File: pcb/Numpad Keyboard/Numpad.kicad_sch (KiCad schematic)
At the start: 57 parts, among them U1 MCP23S17_SO, U2 IS31FL3743-QF

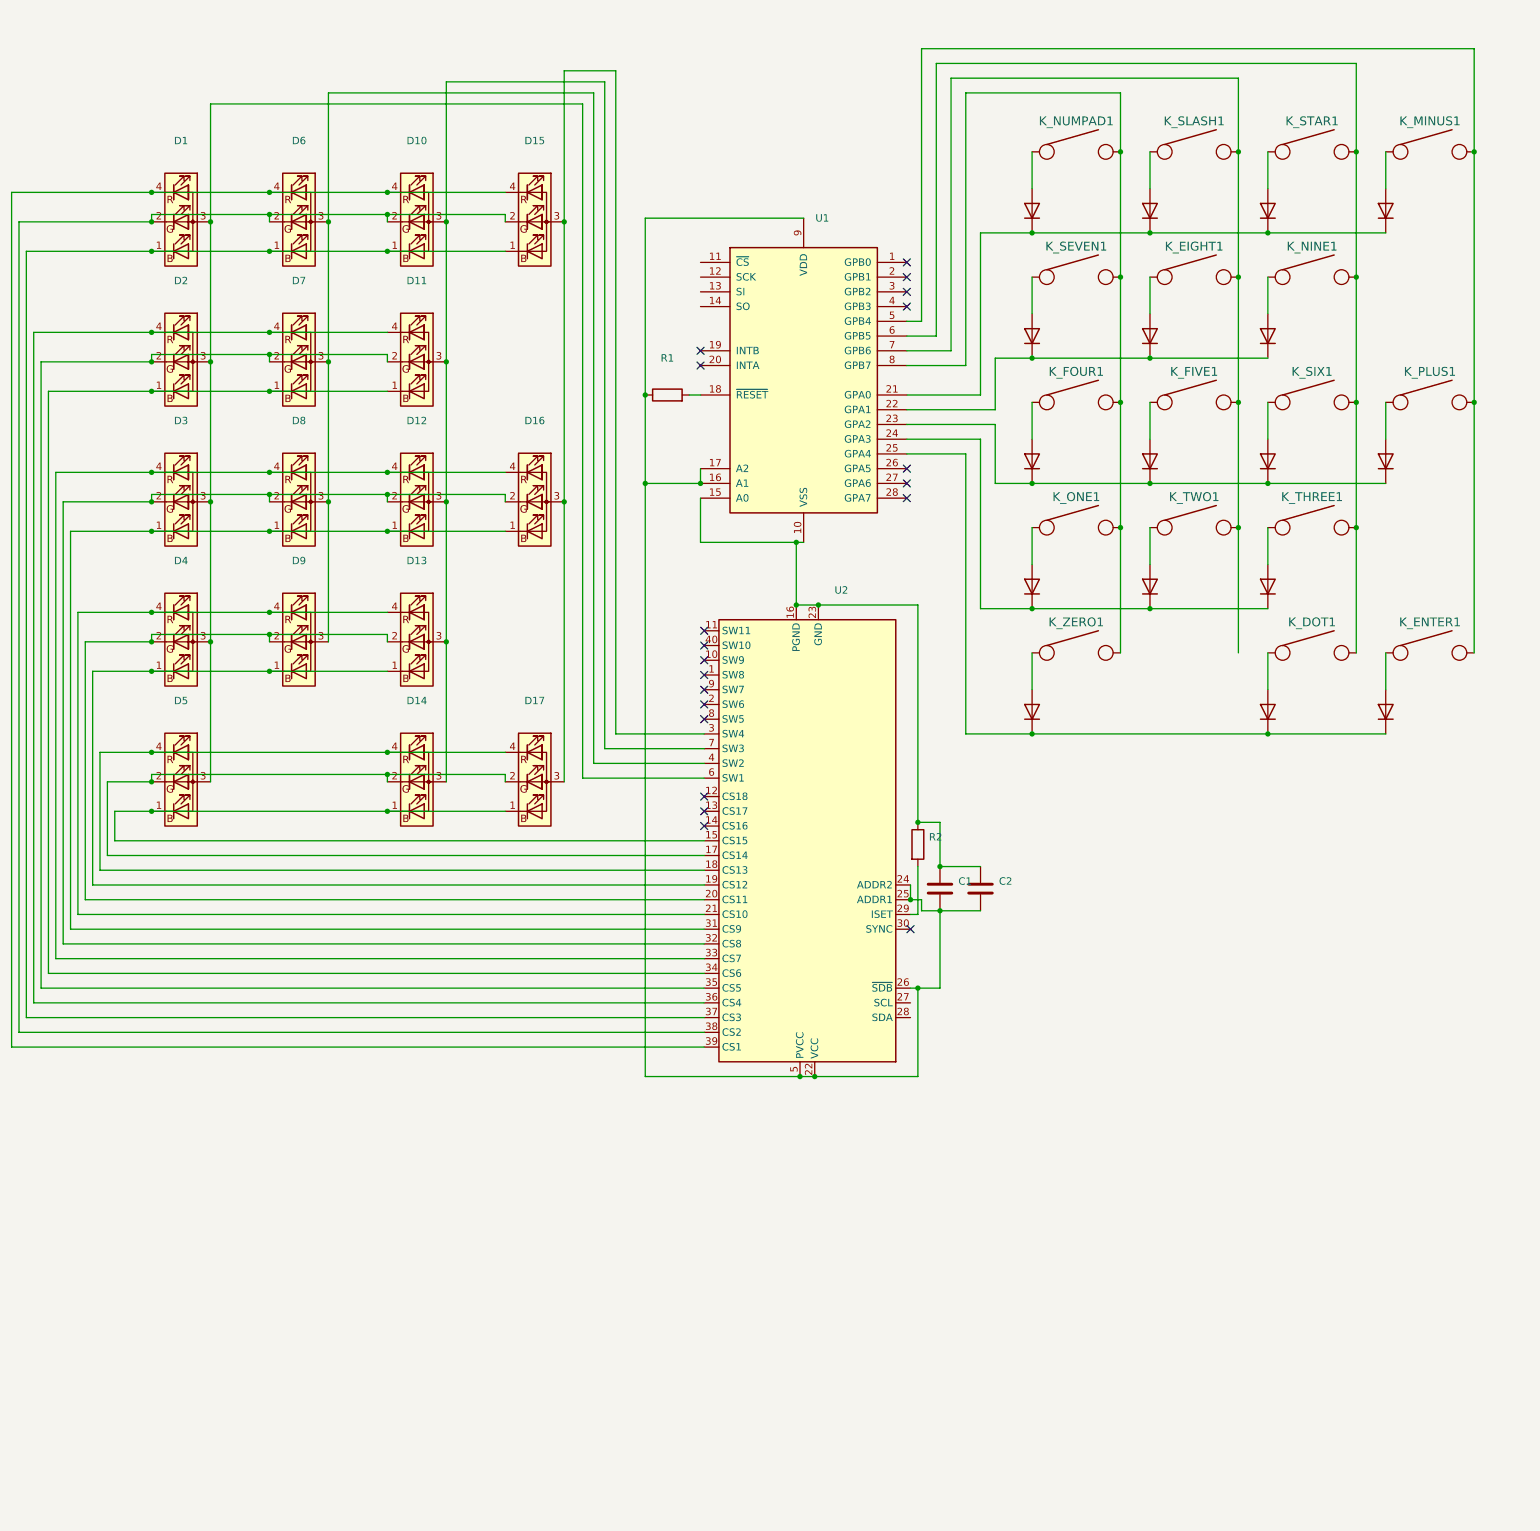
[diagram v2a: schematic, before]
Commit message: Added second LED controller for higher current per LED
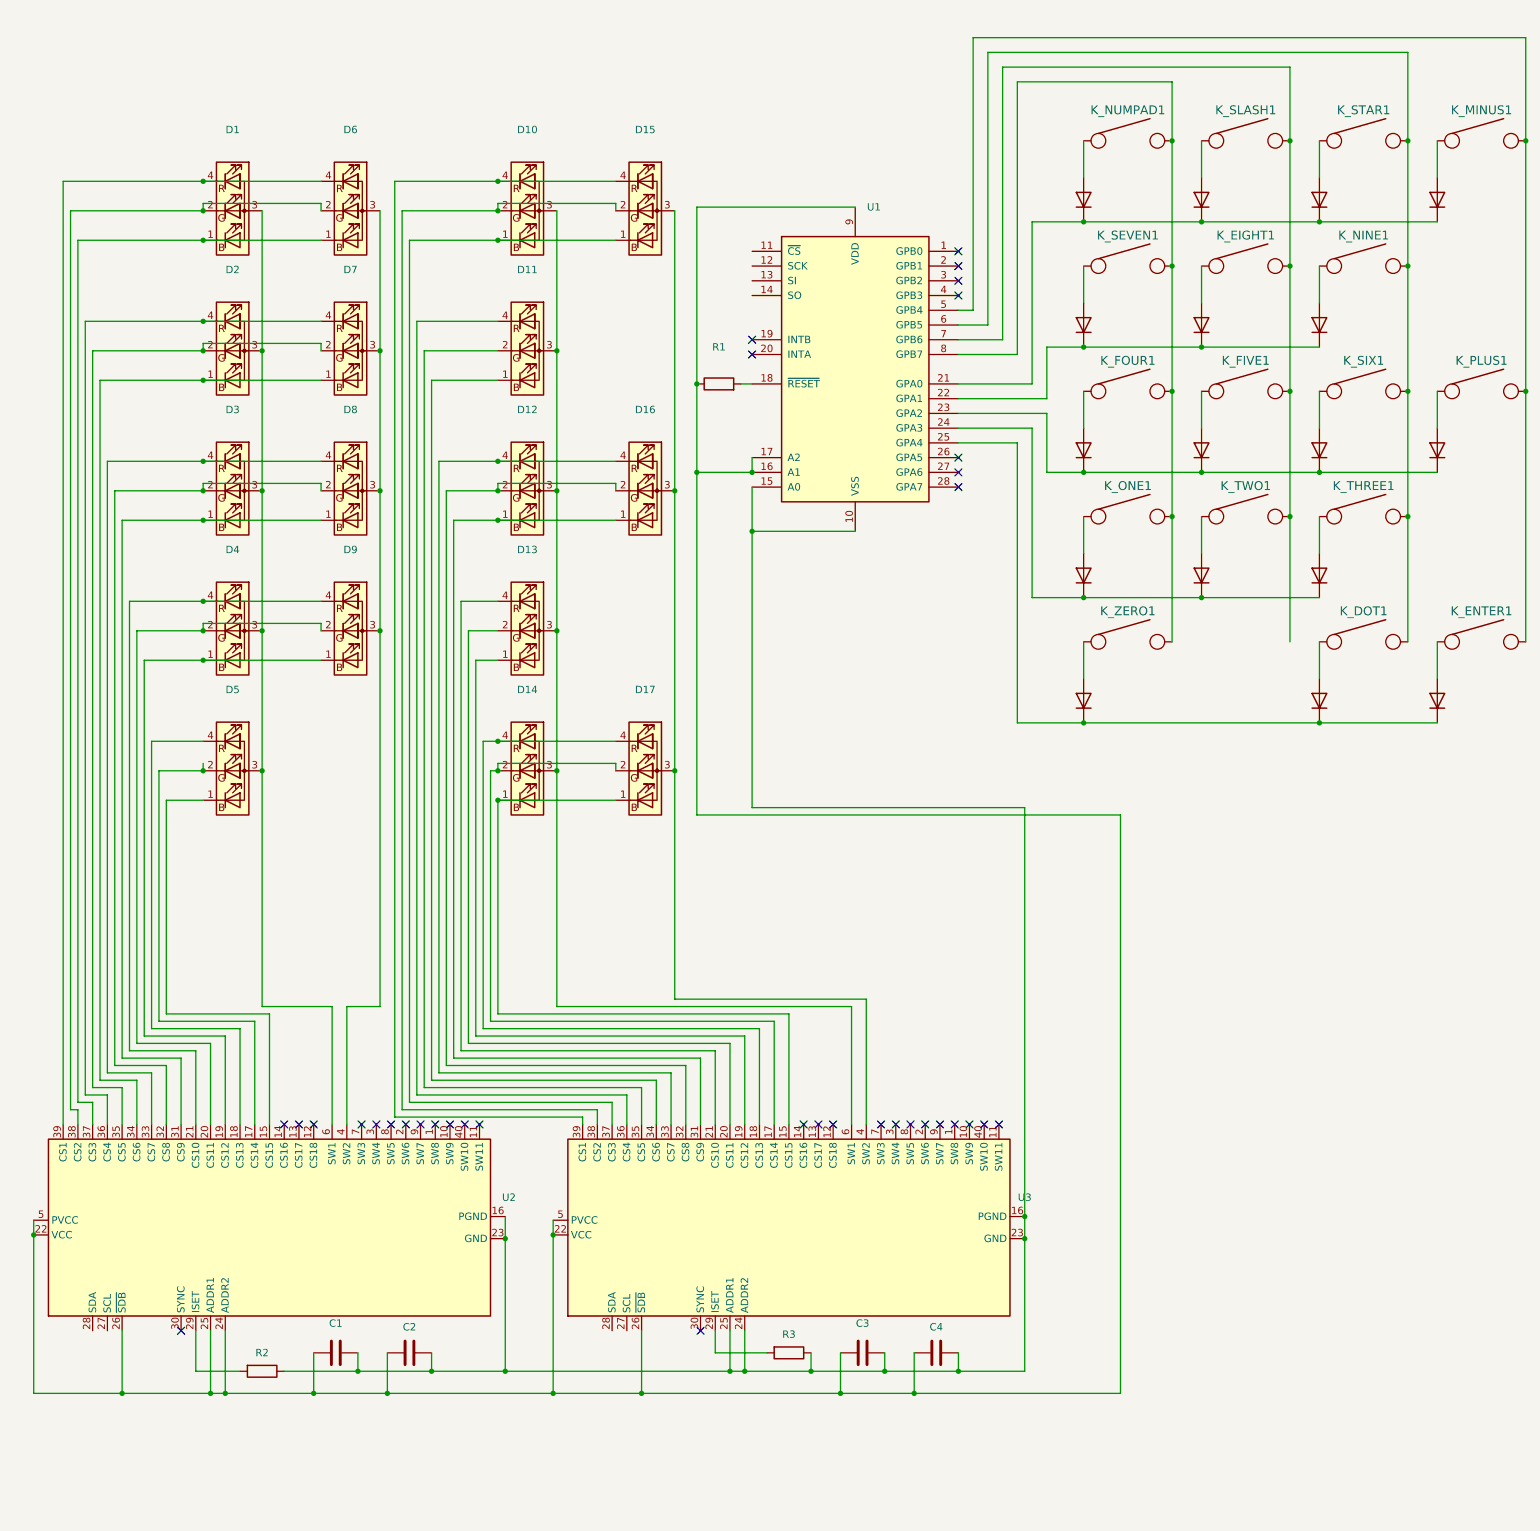
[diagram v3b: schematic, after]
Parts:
- added C3: C 1uF, Footprints:C_0402_1005Metric, symbol vakeyboard:C 1uF
- added C4: C_100nF, Footprints:C_0402_1005Metric, symbol vakeyboard:C_100nF
- added R3: R, Footprints:R_0402_1005Metric, symbol vakeyboard:R
- added U3: IS31FL3743-QF, Footprints:QFN-40-1EP_5x5mm_P0.4mm_EP3.4x3.4mm, symbol vakeyboard:IS31FL3743-QF
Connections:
- net at D1.1 (BK), D6.1 (BK), U2.37 (CS3): no longer D10.1 (BK), D15.1 (BK)
- net at D1.2 (GK), D6.2 (GK), U2.38 (CS2): no longer D10.2 (GK), D15.2 (GK)
- net at D1.4 (RK), D6.4 (RK), U2.39 (CS1): no longer D10.4 (RK), D15.4 (RK)
- net at D2.1 (BK), D7.1 (BK), U2.34 (CS6): no longer D11.1 (BK)
- net at D2.2 (GK), D7.2 (GK), U2.35 (CS5): no longer D11.2 (GK)
- net at D2.4 (RK), D7.4 (RK), U2.36 (CS4): no longer D11.4 (RK)
- net at D15.3 (A), D16.3 (A), D17.3 (A): now also U3.4 (SW2); no longer U2.3 (SW4)
- net at D3.1 (BK), D8.1 (BK), U2.31 (CS9): no longer D12.1 (BK), D16.1 (BK)
- net at D3.2 (GK), D8.2 (GK), U2.32 (CS8): no longer D12.2 (GK), D16.2 (GK)
- net at D3.4 (RK), D8.4 (RK), U2.33 (CS7): no longer D12.4 (RK), D16.4 (RK)
- net at D4.1 (BK), D9.1 (BK), U2.19 (CS12): no longer D13.1 (BK)
- net at D4.2 (GK), D9.2 (GK), U2.20 (CS11): no longer D13.2 (GK)
- net at D4.4 (RK), D9.4 (RK), U2.21 (CS10): no longer D13.4 (RK)
- net at R2.1, U1.10 (VSS), U1.15 (A0)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: now also C1.2, C2.2, C3.2, C4.2, R3.1, U3.16 (PGND), U3.23 (GND), U3.24 (ADDR2), U3.25 (ADDR1); no longer C1.1, C2.1
- net at R1.1, U1.16 (A1), U1.17 (A2)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: now also C1.1, C2.1, C3.1, C4.1, U3.22 (VCC), U3.26 (~{SDB}), U3.5 (PVCC); no longer C1.2, C2.2
- net at D10.3 (A), D11.3 (A), D12.3 (A)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: now also U3.6 (SW1); no longer U2.7 (SW3)
- net at D14.1 (BK), D17.1 (BK): now also U3.15 (CS15); no longer D5.1 (BK), U2.15 (CS15)
- net at D14.2 (GK), D17.2 (GK): now also U3.17 (CS14); no longer D5.2 (GK), U2.17 (CS14)
- net at D14.4 (RK), D17.4 (RK): now also U3.18 (CS13); no longer D5.4 (RK), U2.18 (CS13)
- new net: D10.1 (BK), D15.1 (BK), U3.37 (CS3)
- new net: D10.2 (GK), D15.2 (GK), U3.38 (CS2)
- new net: D10.4 (RK), D15.4 (RK), U3.39 (CS1)
- new net: D12.1 (BK), D16.1 (BK), U3.31 (CS9)
- new net: D12.2 (GK), D16.2 (GK), U3.32 (CS8)
- new net: D12.4 (RK), D16.4 (RK), U3.33 (CS7)
- new net: R3.2, U3.29 (ISET)
- new net: D11.1 (BK), U3.34 (CS6)
- new net: D11.2 (GK), U3.35 (CS5)
- new net: D11.4 (RK), U3.36 (CS4)
- new net: D13.1 (BK), U3.19 (CS12)
- new net: D13.2 (GK), U3.20 (CS11)
- new net: D13.4 (RK), U3.21 (CS10)
- new net: D5.1 (BK), U2.15 (CS15)
- new net: D5.2 (GK), U2.17 (CS14)
- new net: D5.4 (RK), U2.18 (CS13)
- no-connect marks 20 -> 35
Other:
- moved on the sheet: C1, C2, D1, D10, D11, D12, D13, D14, D15, D16, D17, D2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

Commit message: Numpad has all tracks now.
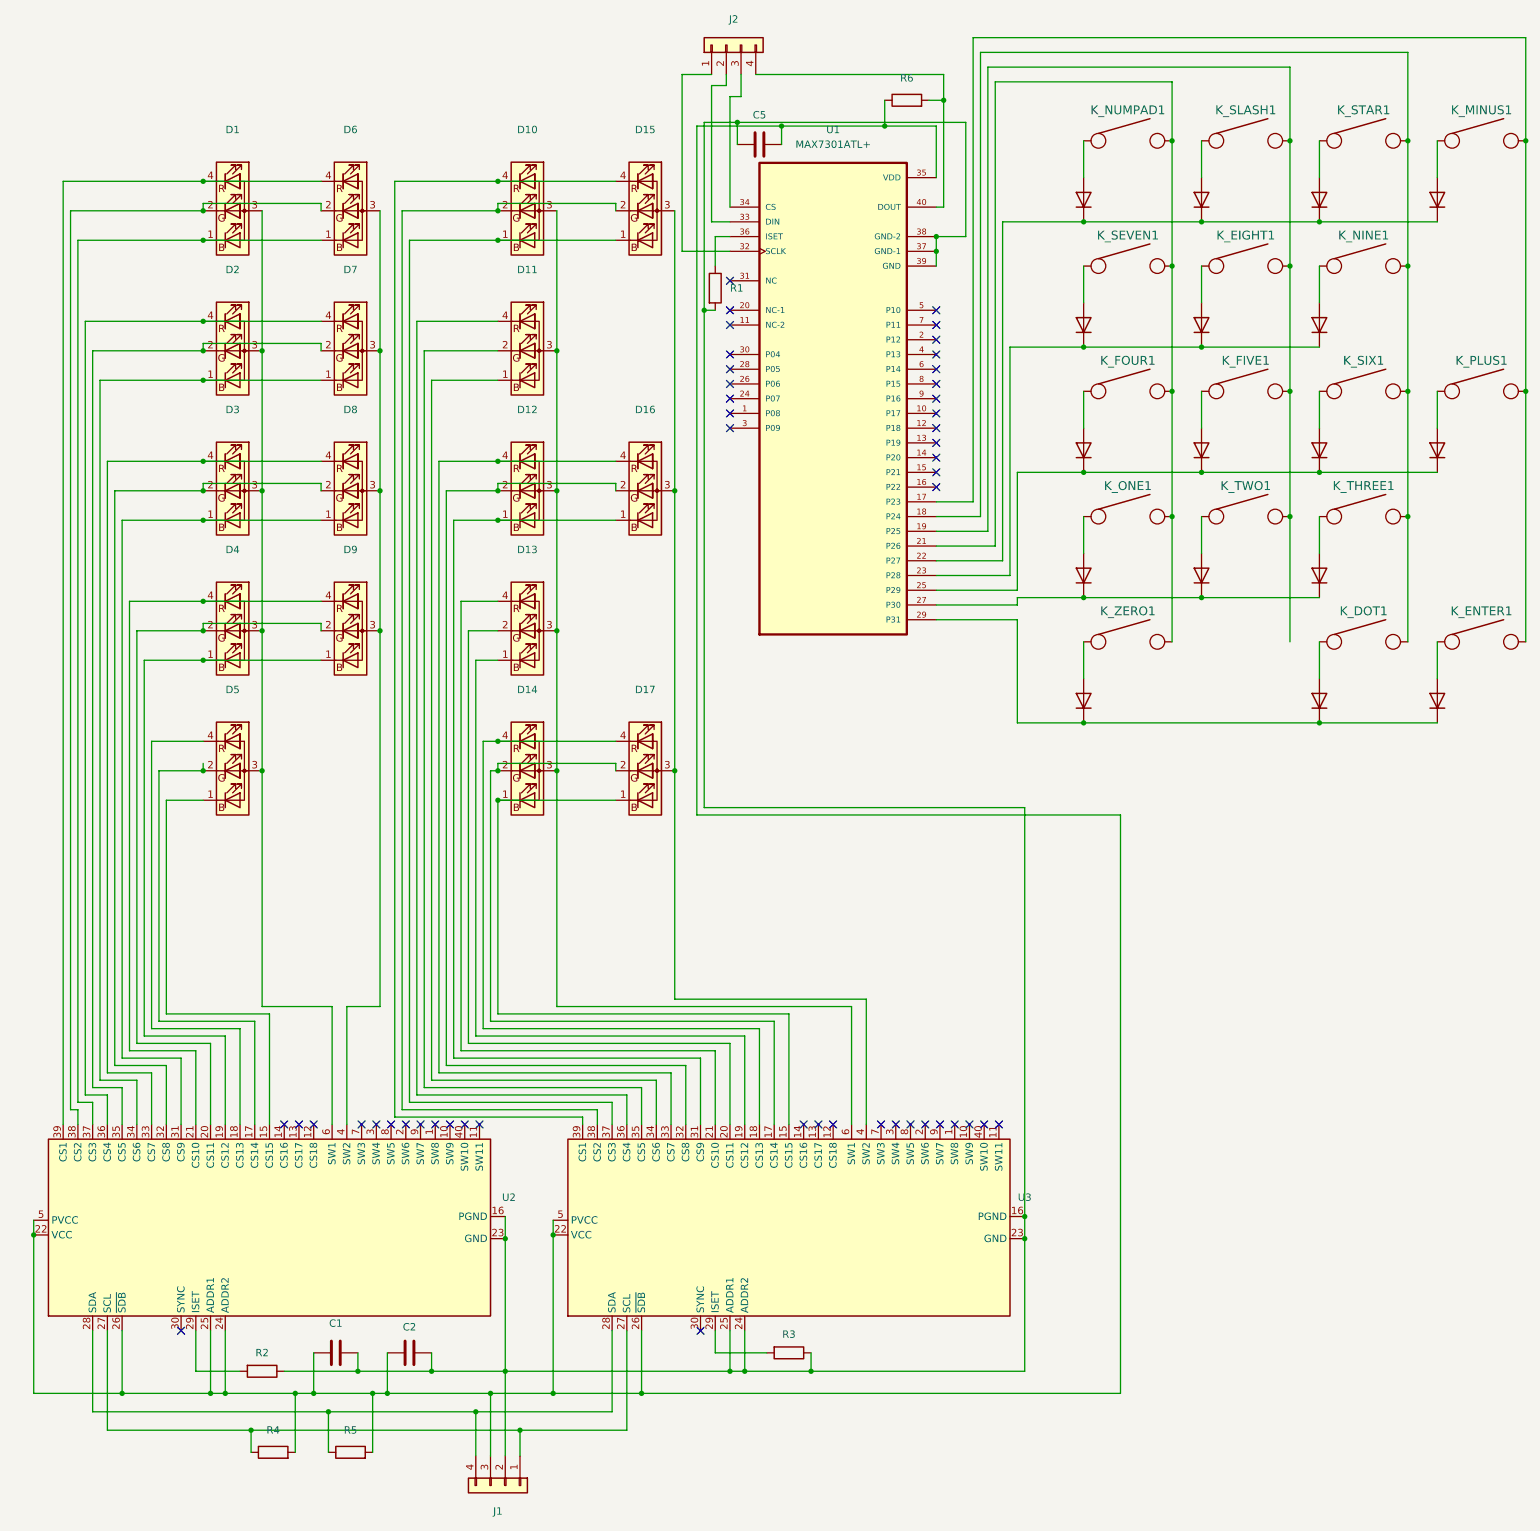
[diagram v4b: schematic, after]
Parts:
- removed C3: C 1uF, Footprints:C_0402_1005Metric, symbol vakeyboard:C 1uF
- removed C4: C_100nF, Footprints:C_0402_1005Metric, symbol vakeyboard:C_100nF
- removed R1: R, Footprints:R_0402_1005Metric, symbol vakeyboard:R
- removed U1: MCP23S17_SO, Package_SO:SOIC-28W_7.5x17.9mm_P1.27mm, symbol vakeyboard:MCP23S17_SO
- added C5: C_47nF, Footprints:C_0402_1005Metric, symbol vakeyboard:C_47nF
- added J1, J2: Conn_01x04, Connector_PinHeader_2.54mm:PinHeader_1x04_P2.54mm_Vertical, symbol vakeyboard:Conn_01x04
- added R1: R_39_kOhm, Footprints:R_0402_1005Metric, symbol vakeyboard:R_39_kOhm
- added R4, R5, R6: R 10 kOhm, Footprints:R_0402_1005Metric, symbol vakeyboard:R 10 kOhm
- added U1: MAX7301ATL+, QFN50P600X600X80-41N, symbol vakeyboard:MAX7301ATL+
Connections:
- net at D19.1 (K), D24.1 (K), D28.1 (K): now also U1.23 (P28)
- net at K_EIGHT1.1, K_FIVE1.1, K_SLASH1.1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: now also U1.19 (P25)
- net at D21.1 (K), D26.1 (K), D30.1 (K): now also U1.27 (P30)
- net at C1.1, C2.1, U2.22 (VCC)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: now also C5.2, J1.3 (Pin_3), R4.2, R5.2, R6.1, U1.35 (VDD)
- net at C1.2, C2.2, R2.1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: now also C5.1, J1.2 (Pin_2), R1.2, U1.37 (GND-1), U1.38 (GND-2), U1.39 (GND)
- net at D18.1 (K), D23.1 (K), D27.1 (K)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: now also U1.22 (P27)
- net at D22.1 (K), D31.1 (K), D34.1 (K): now also U1.29 (P31)
- net at D20.1 (K), D25.1 (K), D29.1 (K)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: now also U1.25 (P29)
- net at K_ENTER1.1, K_MINUS1.1, K_PLUS1.1: now also U1.17 (P23)
- net at K_DOT1.1, K_NINE1.1, K_SIX1.1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: now also U1.18 (P24)
- net at K_FOUR1.1, K_NUMPAD1.1, K_ONE1.1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: now also U1.21 (P26)
- net at U2.27 (SCL): now also U3.27 (SCL), J1.1 (Pin_1), R4.1
- net at U2.28 (SDA): now also U3.28 (SDA), J1.4 (Pin_4), R5.1
- new net: R1.1, U1.36 (ISET)
- new net: J2.1 (Pin_1), U1.32 (SCLK)
- new net: J2.2 (Pin_2), U1.33 (DIN)
- new net: J2.3 (Pin_3), U1.34 (CS)
- new net: J2.4 (Pin_4), R6.2, U1.40 (DOUT)
- no-connect marks 35 -> 48

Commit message: Fixed fields
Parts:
- J1, J2: Mfg Part # (none) -> BG302-04-A-L-G; Mfg part # BG302-04-A-L-G -> (none)
- U1: Description / Value (none) -> TQFN-40_EP(6x6) I/O Expanders ROHS; LCSC (none) -> C1522600; Manufacturer (none) -> Maxim Integrated; Mfg Part # (none) -> MAX7301ATL+; Package/Footprint (none) -> TQFN-40; Type (none) -> SMD
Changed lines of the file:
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@@
-      (effects (font (size 1.27 1.27)) hide)
-    )
-    (property "Mfg part #" "BG302-04-A-L-G" (id 5) (at 99.695 264.16 0)
       (effects (font (size 1.27 1.27)) hide)
     )
@@
     )
     (property "Your Instructions / Notes" "Connector will be mounted from back of PCB. Please rotate in a way, that cable will be plugged from closer edge of PCB." (id 10) (at 99.695 264.16 0)
+      (effects (font (size 1.27 1.27)) hide)
+    )
+    (property "Mfg Part #" "BG302-04-A-L-G" (id 11) (at 99.695 264.16 0)
       (effects (font (size 1.27 1.27)) hide)
     )
@@
       (effects (font (size 1.27 1.27)) (justify left bottom) hide)
     )
-    (property "Datasheet" "" (id 3) (at 156.21 76.835 0)
+    (property "Datasheet" "https://cz.mouser.com/datasheet/2/256/MAX7301-1516196.pdf" (id 3) (at 156.21 76.835 0)
       (effects (font (size 1.27 1.27)) (justify left bottom) hide)
+    )
+    (property "Description / Value" "TQFN-40_EP(6x6)  I/O Expanders ROHS" (id 4) (at 156.21 76.835 0)
+      (effects (font (size 1.27 1.27)) hide)
+    )
+    (property "LCSC" "C1522600" (id 5) (at 156.21 76.835 0)
+      (effects (font (size 1.27 1.27)) hide)
+    )
+    (property "Manufacturer" "Maxim Integrated" (id 6) (at 156.21 76.835 0)
+      (effects (font (size 1.27 1.27)) hide)
+    )
+    (property "Mfg Part #" "MAX7301ATL+" (id 7) (at 156.21 76.835 0)
+      (effects (font (size 1.27 1.27)) hide)
+    )
+    (property "Package/Footprint" "TQFN-40" (id 8) (at 156.21 76.835 0)
+      (effects (font (size 1.27 1.27)) hide)
+    )
+    (property "Type" "SMD" (id 9) (at 156.21 76.835 0)
+      (effects (font (size 1.27 1.27)) hide)
     )
     (pin "1")
@@
       (effects (font (size 1.27 1.27)) hide)
     )
-    (property "Mfg part #" "BG302-04-A-L-G" (id 5) (at 137.795 15.875 0)
-      (effects (font (size 1.27 1.27)) hide)
-    )
     (property "Manufacturer" "GCT (GLOBAL CONNECTOR TECHNOLOGY)" (id 6) (at 137.795 15.875 0)
       (effects (font (size 1.27 1.27)) hide)
@@
       (effects (font (size 1.27 1.27)) hide)
     )
+    (property "Mfg Part #" "BG302-04-A-L-G" (id 11) (at 137.795 15.875 0)
+      (effects (font (size 1.27 1.27)) hide)
+    )
